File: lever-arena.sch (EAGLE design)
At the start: 24 parts, among them J1 POWER_JACKPTH_BREAD

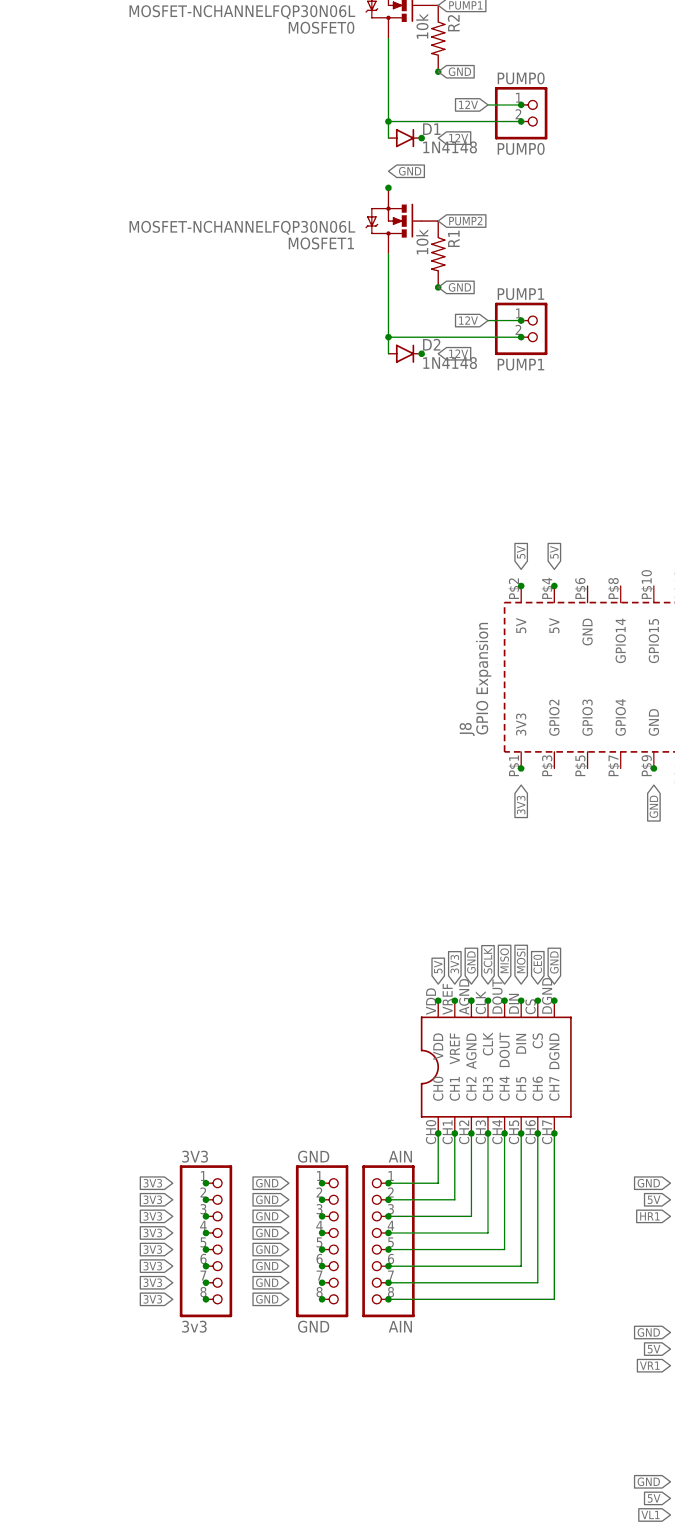
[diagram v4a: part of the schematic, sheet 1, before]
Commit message: added labels
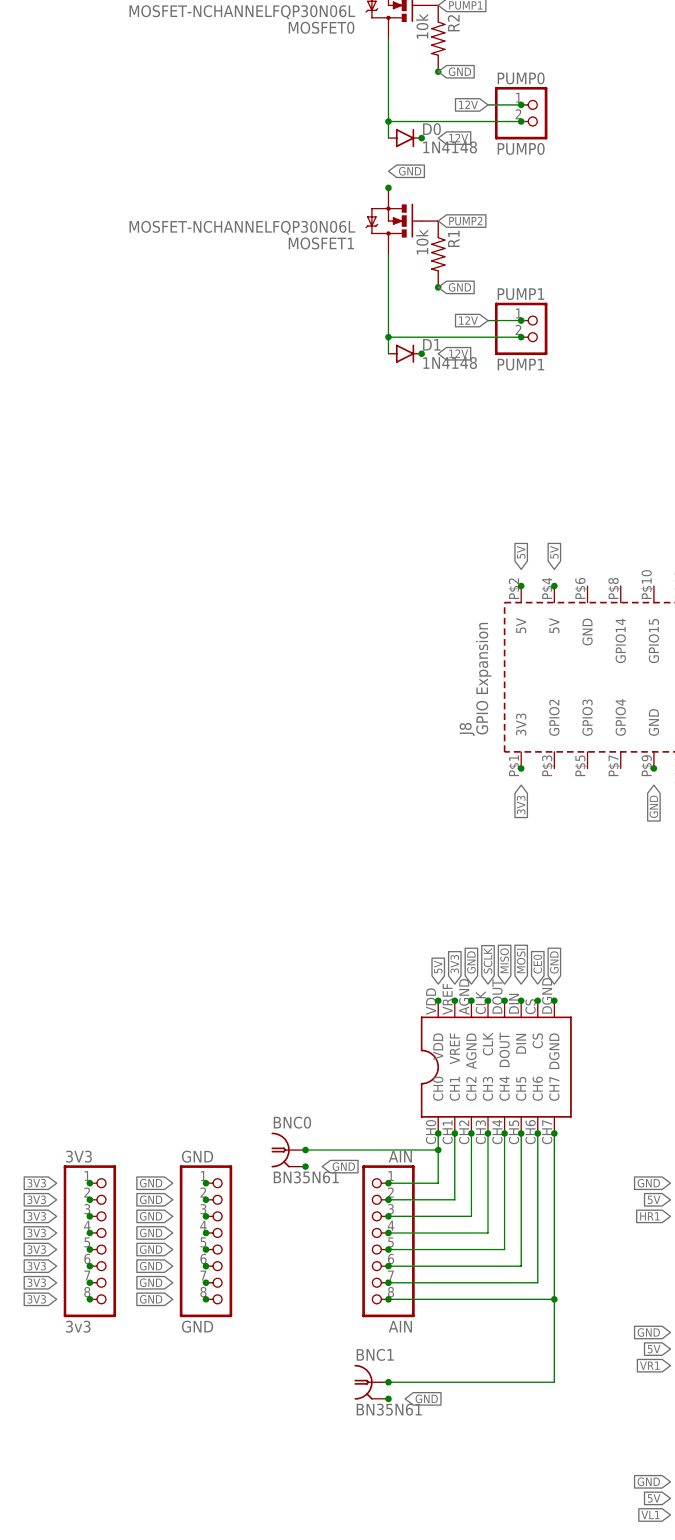
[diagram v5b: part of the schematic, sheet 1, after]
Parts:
- removed D2: 1N4148, SparkFun-DiscreteSemi:DIODE1N4148
- added BNC0, BNC1: BN35N61, con-coax:BN35N61
- added D0: 1N4148, SparkFun-DiscreteSemi:DIODE1N4148
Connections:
- removed net N$1: ADC0.CH0, AIN.1
- removed net N$17: ADC0.CH7, AIN.8
- new net N$3: ADC0.CH0, AIN.1, BNC0.1
- new net N$6: ADC0.CH7, AIN.8, BNC1.1
- net 12V: now also D0.C, D1.A; no longer D2.A, D2.C
- net GND: now also BNC0.2, BNC1.2
- net N$4: now also D0.A; no longer D1.A
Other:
- moved on the sheet: 3V3, D1, GND
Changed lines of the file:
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@@
 <part name="PUMP1" library="pinhead" deviceset="PINHD-1X2" device="" value="PUMP1"/>
 <part name="PUMP0" library="pinhead" deviceset="PINHD-1X2" device="" value="PUMP0"/>
+<part name="D0" library="SparkFun-DiscreteSemi" deviceset="DIODE" device="1N4148" value="1N4148"/>
 <part name="D1" library="SparkFun-DiscreteSemi" deviceset="DIODE" device="1N4148" value="1N4148"/>
-<part name="D2" library="SparkFun-DiscreteSemi" deviceset="DIODE" device="1N4148" value="1N4148"/>
 <part name="HL1" library="pinhead" deviceset="PINHD-1X6" device="" value="HL1"/>
 <part name="VL1" library="pinhead" deviceset="PINHD-1X6" device="" value="VL1"/>
@@
 <part name="AIN" library="pinhead" deviceset="PINHD-1X8" device="" value="AIN"/>
 <part name="3V3" library="pinhead" deviceset="PINHD-1X8" device="" value="3v3"/>
+<part name="BNC0" library="con-coax" deviceset="BN35N61" device=""/>
+<part name="BNC1" library="con-coax" deviceset="BN35N61" device=""/>
 </parts>
 <sheets>
@@
 <instance part="PUMP1" gate="G$1" x="-45.72" y="53.34"/>
 <instance part="PUMP0" gate="G$1" x="-45.72" y="86.36"/>
-<instance part="D1" gate="G$1" x="-66.04" y="83.82"/>
-<instance part="D2" gate="G$1" x="-66.04" y="50.8"/>
+<instance part="D0" gate="G$1" x="-66.04" y="83.82"/>
+<instance part="D1" gate="G$1" x="-66.04" y="50.8"/>
 <instance part="HL1" gate="A" x="-22.86" y="-152.4" rot="MR0"/>
 <instance part="VL1" gate="A" x="-22.86" y="-129.54" rot="MR0"/>
@@
 <instance part="VR0" gate="A" x="17.78" y="-127" rot="MR180"/>
 <instance part="HR0" gate="A" x="17.78" y="-149.86" rot="MR180"/>
-<instance part="GND" gate="A" x="-76.2" y="-86.36"/>
+<instance part="GND" gate="A" x="-93.98" y="-86.36"/>
 <instance part="AIN" gate="A" x="-71.12" y="-86.36" rot="MR0"/>
-<instance part="3V3" gate="A" x="-93.98" y="-86.36"/>
+<instance part="3V3" gate="A" x="-111.76" y="-86.36"/>
+<instance part="BNC0" gate="G$1" x="-83.82" y="-71.12"/>
+<instance part="BNC1" gate="G$1" x="-71.12" y="-106.68"/>
 </instances>
 <busses>
@@
 <segment>
 <pinref part="GND" gate="A" pin="1"/>
-<junction x="-78.74" y="-76.2"/>
-<label x="-83.82" y="-76.2" size="1.27" layer="95" rot="R180" xref="yes"/>
+<junction x="-96.52" y="-76.2"/>
+<label x="-101.6" y="-76.2" size="1.27" layer="95" rot="R180" xref="yes"/>
 </segment>
 <segment>
 <pinref part="GND" gate="A" pin="2"/>
-<junction x="-78.74" y="-78.74"/>
-<label x="-83.82" y="-78.74" size="1.27" layer="95" rot="R180" xref="yes"/>
+<junction x="-96.52" y="-78.74"/>
+<label x="-101.6" y="-78.74" size="1.27" layer="95" rot="R180" xref="yes"/>
 </segment>
 <segment>
 <pinref part="GND" gate="A" pin="3"/>
-<junction x="-78.74" y="-81.28"/>
-<label x="-83.82" y="-81.28" size="1.27" layer="95" rot="R180" xref="yes"/>
+<junction x="-96.52" y="-81.28"/>
+<label x="-101.6" y="-81.28" size="1.27" layer="95" rot="R180" xref="yes"/>
 </segment>
 <segment>
 <pinref part="GND" gate="A" pin="5"/>
-<junction x="-78.74" y="-86.36"/>
-<label x="-83.82" y="-86.36" size="1.27" layer="95" rot="R180" xref="yes"/>
+<junction x="-96.52" y="-86.36"/>
+<label x="-101.6" y="-86.36" size="1.27" layer="95" rot="R180" xref="yes"/>
 </segment>
 <segment>
 <pinref part="GND" gate="A" pin="4"/>
-<junction x="-78.74" y="-83.82"/>
-<label x="-83.82" y="-83.82" size="1.27" layer="95" rot="R180" xref="yes"/>
+<junction x="-96.52" y="-83.82"/>
+<label x="-101.6" y="-83.82" size="1.27" layer="95" rot="R180" xref="yes"/>
 </segment>
 <segment>
 <pinref part="GND" gate="A" pin="6"/>
-<junction x="-78.74" y="-88.9"/>
-<label x="-83.82" y="-88.9" size="1.27" layer="95" rot="R180" xref="yes"/>
+<junction x="-96.52" y="-88.9"/>
+<label x="-101.6" y="-88.9" size="1.27" layer="95" rot="R180" xref="yes"/>
 </segment>
 <segment>
 <pinref part="GND" gate="A" pin="7"/>
-<junction x="-78.74" y="-91.44"/>
-<label x="-83.82" y="-91.44" size="1.27" layer="95" rot="R180" xref="yes"/>
+<junction x="-96.52" y="-91.44"/>
+<label x="-101.6" y="-91.44" size="1.27" layer="95" rot="R180" xref="yes"/>
 </segment>
 <segment>
 <pinref part="GND" gate="A" pin="8"/>
-<junction x="-78.74" y="-93.98"/>
-<label x="-83.82" y="-93.98" size="1.27" layer="95" rot="R180" xref="yes"/>
+<junction x="-96.52" y="-93.98"/>
+<label x="-101.6" y="-93.98" size="1.27" layer="95" rot="R180" xref="yes"/>
+</segment>
+<segment>
+<pinref part="BNC0" gate="G$1" pin="2"/>
+<junction x="-81.28" y="-73.66"/>
+<label x="-78.74" y="-73.66" size="1.27" layer="95" xref="yes"/>
+</segment>
+<segment>
+<pinref part="BNC1" gate="G$1" pin="2"/>
+<junction x="-68.58" y="-109.22"/>
+<label x="-66.04" y="-109.22" size="1.27" layer="95" xref="yes"/>
 </segment>
 </net>
@@
 <segment>
 <pinref part="3V3" gate="A" pin="1"/>
-<junction x="-96.52" y="-76.2"/>
-<label x="-101.6" y="-76.2" size="1.27" layer="95" rot="R180" xref="yes"/>
+<junction x="-114.3" y="-76.2"/>
+<label x="-119.38" y="-76.2" size="1.27" layer="95" rot="R180" xref="yes"/>
 </segment>
 <segment>
 <pinref part="3V3" gate="A" pin="2"/>
-<junction x="-96.52" y="-78.74"/>
-<label x="-101.6" y="-78.74" size="1.27" layer="95" rot="R180" xref="yes"/>
+<junction x="-114.3" y="-78.74"/>
+<label x="-119.38" y="-78.74" size="1.27" layer="95" rot="R180" xref="yes"/>
 </segment>
 <segment>
 <pinref part="3V3" gate="A" pin="3"/>
-<junction x="-96.52" y="-81.28"/>
-<label x="-101.6" y="-81.28" size="1.27" layer="95" rot="R180" xref="yes"/>
+<junction x="-114.3" y="-81.28"/>
+<label x="-119.38" y="-81.28" size="1.27" layer="95" rot="R180" xref="yes"/>
 </segment>
 <segment>
 <pinref part="3V3" gate="A" pin="4"/>
-<junction x="-96.52" y="-83.82"/>
-<label x="-101.6" y="-83.82" size="1.27" layer="95" rot="R180" xref="yes"/>
+<junction x="-114.3" y="-83.82"/>
+<label x="-119.38" y="-83.82" size="1.27" layer="95" rot="R180" xref="yes"/>
 </segment>
 <segment>
 <pinref part="3V3" gate="A" pin="5"/>
-<junction x="-96.52" y="-86.36"/>
-<label x="-101.6" y="-86.36" size="1.27" layer="95" rot="R180" xref="yes"/>
+<junction x="-114.3" y="-86.36"/>
+<label x="-119.38" y="-86.36" size="1.27" layer="95" rot="R180" xref="yes"/>
 </segment>
 <segment>
 <pinref part="3V3" gate="A" pin="6"/>
-<junction x="-96.52" y="-88.9"/>
-<label x="-101.6" y="-88.9" size="1.27" layer="95" rot="R180" xref="yes"/>
+<junction x="-114.3" y="-88.9"/>
+<label x="-119.38" y="-88.9" size="1.27" layer="95" rot="R180" xref="yes"/>
 </segment>
 <segment>
 <pinref part="3V3" gate="A" pin="7"/>
-<junction x="-96.52" y="-91.44"/>
-<label x="-101.6" y="-91.44" size="1.27" layer="95" rot="R180" xref="yes"/>
+<junction x="-114.3" y="-91.44"/>
+<label x="-119.38" y="-91.44" size="1.27" layer="95" rot="R180" xref="yes"/>
 </segment>
 <segment>
 <pinref part="3V3" gate="A" pin="8"/>
-<junction x="-96.52" y="-93.98"/>
-<label x="-101.6" y="-93.98" size="1.27" layer="95" rot="R180" xref="yes"/>
+<junction x="-114.3" y="-93.98"/>
+<label x="-119.38" y="-93.98" size="1.27" layer="95" rot="R180" xref="yes"/>
 </segment>
 <segment>
@@
 </segment>
 <segment>
-<pinref part="D1" gate="G$1" pin="C"/>
+<pinref part="D0" gate="G$1" pin="C"/>
 <junction x="-63.5" y="83.82"/>
 <label x="-60.96" y="83.82" size="1.27" layer="95" xref="yes"/>
@@
 <wire x1="-68.58" y1="53.34" x2="-68.58" y2="66.04" width="0.1524" layer="91"/>
 <wire x1="-48.26" y1="53.34" x2="-68.58" y2="53.34" width="0.1524" layer="91"/>
-<pinref part="D2" gate="G$1" pin="A"/>
+<pinref part="D1" gate="G$1" pin="A"/>
 <wire x1="-68.58" y1="53.34" x2="-68.58" y2="50.8" width="0.1524" layer="91"/>
 <junction x="-68.58" y="53.34"/>
 </segment>
 <segment>
-<pinref part="D2" gate="G$1" pin="C"/>
+<pinref part="D1" gate="G$1" pin="C"/>
 <junction x="-63.5" y="50.8"/>
 <label x="-60.96" y="50.8" size="1.27" layer="95" xref="yes"/>
@@
 <wire x1="-68.58" y1="86.36" x2="-68.58" y2="99.06" width="0.1524" layer="91"/>
 <wire x1="-48.26" y1="86.36" x2="-68.58" y2="86.36" width="0.1524" layer="91"/>
-<pinref part="D1" gate="G$1" pin="A"/>
+<pinref part="D0" gate="G$1" pin="A"/>
 <wire x1="-68.58" y1="86.36" x2="-68.58" y2="83.82" width="0.1524" layer="91"/>
 <junction x="-68.58" y="86.36"/>
@@
 </segment>
 </net>
-<net name="N$1" class="0">
-<segment>
-<pinref part="AIN" gate="A" pin="1"/>
-<junction x="-68.58" y="-76.2"/>
-<pinref part="ADC0" gate="MCP3208$1" pin="CH0"/>
-<junction x="-60.96" y="-68.58"/>
-<wire x1="-68.58" y1="-76.2" x2="-60.96" y2="-76.2" width="0.1524" layer="91"/>
-<wire x1="-60.96" y1="-76.2" x2="-60.96" y2="-68.58" width="0.1524" layer="91"/>
-</segment>
-</net>
 <net name="N$11" class="0">
 <segment>
@@
 </segment>
 </net>
-<net name="N$17" class="0">
-<segment>
+<net name="N$3" class="0">
+<segment>
+<pinref part="BNC0" gate="G$1" pin="1"/>
+<junction x="-81.28" y="-71.12"/>
+<pinref part="AIN" gate="A" pin="1"/>
+<junction x="-68.58" y="-76.2"/>
+<pinref part="ADC0" gate="MCP3208$1" pin="CH0"/>
+<junction x="-60.96" y="-68.58"/>
+<wire x1="-68.58" y1="-76.2" x2="-60.96" y2="-76.2" width="0.1524" layer="91"/>
+<wire x1="-60.96" y1="-76.2" x2="-60.96" y2="-71.12" width="0.1524" layer="91"/>
+<wire x1="-60.96" y1="-71.12" x2="-60.96" y2="-68.58" width="0.1524" layer="91"/>
+<wire x1="-81.28" y1="-71.12" x2="-60.96" y2="-71.12" width="0.1524" layer="91"/>
+<junction x="-60.96" y="-71.12"/>
+</segment>
+</net>
+<net name="N$6" class="0">
+<segment>
+<pinref part="BNC1" gate="G$1" pin="1"/>
+<junction x="-68.58" y="-106.68"/>
 <pinref part="AIN" gate="A" pin="8"/>
 <junction x="-68.58" y="-93.98"/>
@@
 <wire x1="-68.58" y1="-93.98" x2="-43.18" y2="-93.98" width="0.1524" layer="91"/>
 <wire x1="-43.18" y1="-93.98" x2="-43.18" y2="-68.58" width="0.1524" layer="91"/>
-</segment>
-</net>
+<wire x1="-68.58" y1="-106.68" x2="-43.18" y2="-106.68" width="0.1524" layer="91"/>
+<wire x1="-43.18" y1="-106.68" x2="-43.18" y2="-93.98" width="0.1524" layer="91"/>
+<junction x="-43.18" y="-93.98"/>
+</segment>
+</net>
